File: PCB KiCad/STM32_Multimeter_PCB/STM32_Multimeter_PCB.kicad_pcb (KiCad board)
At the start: 2 copper layers, 128 parts, among them J1 Conn_01x02_Pin, J10 Conn_01x01_Pin, J11 Conn_01x01_Pin, J2 USB_B_Micro, J3 Conn_01x04_Pin, J4 Conn_Coaxial, J5 Conn_01x03_Pin, J7 Conn_01x02_Pin, J8 Conn_01x01_Pin, K1 G6K-2, Q1 AOD2810, Q10 BC327, Q11 BC327, Q12 BC327, Q13 BC327, Q14 BC327, Q15 BC327, Q2 AOD2810, Q3 AOD2810, Q4 AOD2810, Q5 AOD2810, Q6 BC327, Q7 BC327, Q8 BC327, Q9 BC327, SW1 SW_Push, SW3 SW_Push, SW4 SW_DPDT_x2, U1 STM32WB55CGUx, U10 AMS1117-3.3, U11 4051, U3 LTC4054XES5-4.2, U4 DW01A, U5 FS8205A, U9 TPS61040DBV, Y1 Crystal 32 MHz

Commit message: Routed Analog and Microcontroler section
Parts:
- D7, F1, J11, Q12, Q13, Q14, Q3, Q4, Q5, R16, R17, R18, R19, R25, R26, R38, R4, R41, R42, R43, R44, R45, R46, R47, R48: moved to B.Cu
- J1: footprint Connector_PinHeader_2.54mm:PinHeader_1x02_P2.54mm_Vertical -> moje_elementy:batt
- moved D7 195.8 mm to (76.7, 30.9), turned to 90 degrees
- moved R38 195.5 mm to (73.0, 32.4)
- moved R46 193.9 mm to (85.3, 34.4)
- moved R47 193.7 mm to (85.3, 31.5)
- moved R48 193.7 mm to (85.3, 28.5)
- moved R44 192.8 mm to (64.1, 41.7), turned to 180 degrees
- moved R26 192.5 mm to (64.1, 39.3), turned to 180 degrees
- moved R42 192.4 mm to (51.5, 41.7), turned to 180 degrees
- moved R41 192.4 mm to (38.8, 41.7), turned to 180 degrees
- moved R19 192.2 mm to (38.8, 39.4), turned to 180 degrees
- moved R25 192.1 mm to (51.5, 39.4), turned to 180 degrees
- moved Q12 192.0 mm to (38.9, 45.0), turned to -90 degrees
- moved Q13 189.1 mm to (51.7, 45.2), turned to -90 degrees
- moved Q14 189.0 mm to (64.2, 45.2), turned to -90 degrees
- moved R4 187.8 mm to (39.0, 48.2)
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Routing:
- net Net-(Q3-D): track 0.00 -> 54.4 mm
- net Net-(D4-A2): track 0.00 -> 34.2 mm
- net Net-(Q4-S): track 0.00 -> 29.5 mm
- net VDD: track 9.02 -> 29.8 mm
- net Net-(U1-PH3): track 0.00 -> 20.4 mm
- net +5V: track 0.00 -> 18.2 mm, vias 0 -> 2
- net Net-(J1-Pin_2): track 0.00 -> 18.1 mm
- net Net-(K1-Pad5): track 0.00 -> 16.7 mm
- net Net-(Q5-S): track 0.00 -> 16.3 mm
- net Net-(U1-PB7): track 0.00 -> 15.7 mm
- net Net-(K1-Pad7): track 0.00 -> 13.9 mm
- net Net-(U1-NRST): track 0.00 -> 13.7 mm
- net Net-(Q3-S): track 0.00 -> 12.8 mm
- net Net-(J1-Pin_1): track 0.00 -> 12.4 mm
- net GND: track 5.51 -> 15.8 mm
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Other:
- copper layers 2 -> 4

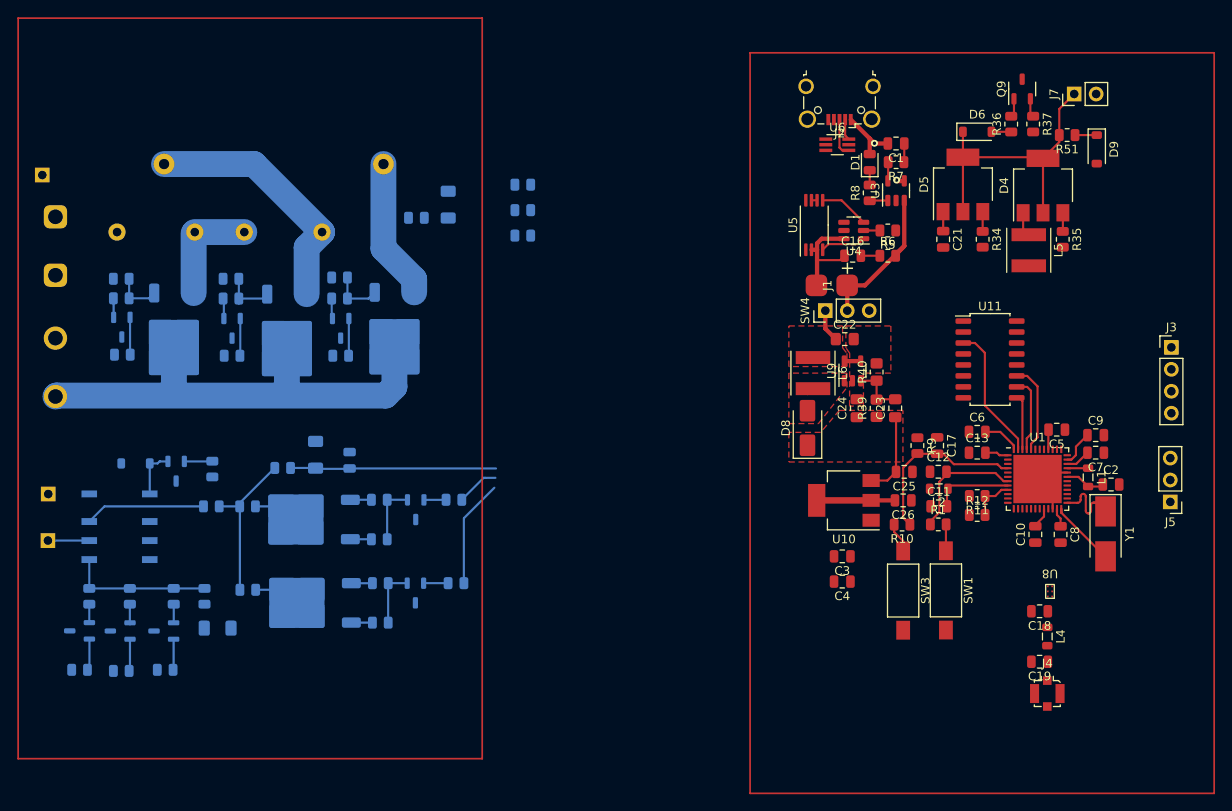
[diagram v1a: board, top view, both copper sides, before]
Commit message: routed out signals and power planes
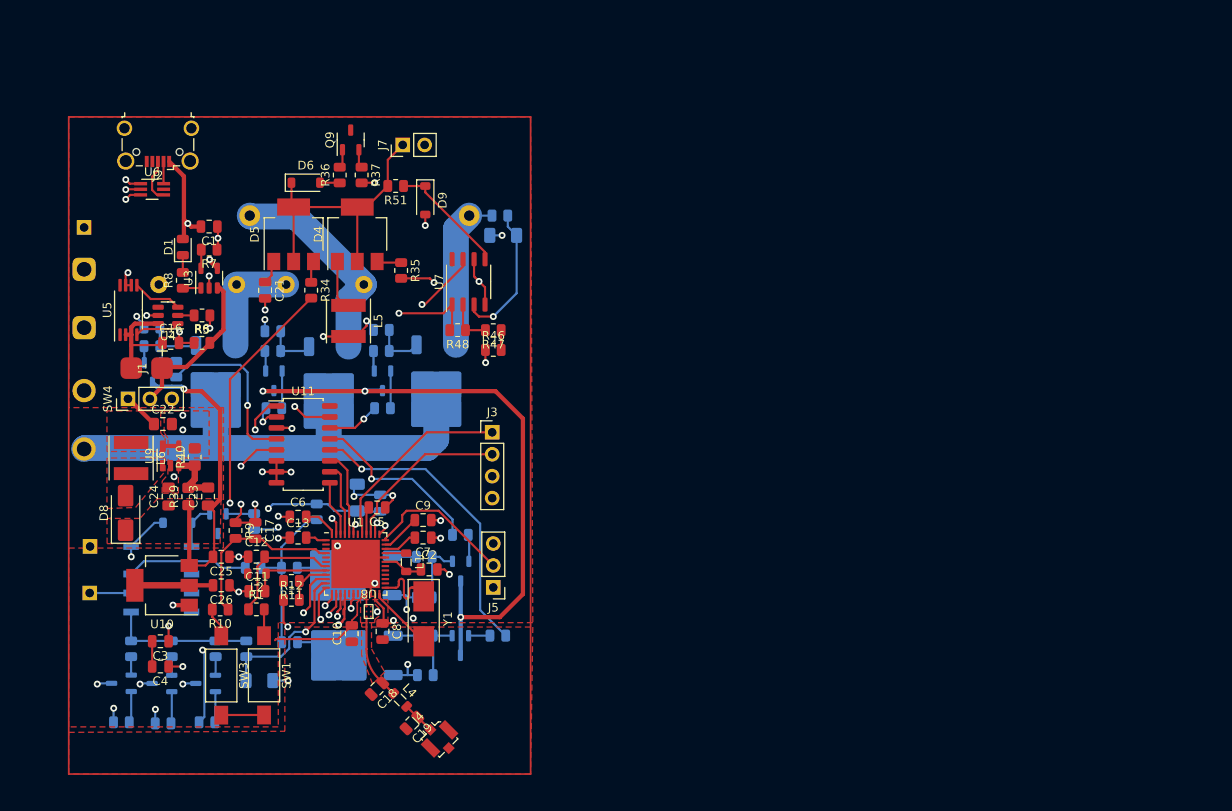
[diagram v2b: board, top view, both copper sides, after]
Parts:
- added U7: ~, Package_SO:SOP-8_3.9x4.9mm_P1.27mm, F.Cu at (79.1, 39.8)
- R46, R47, R48: moved to F.Cu
- moved SW4 81.4 mm to (39.6, 53.3)
- moved C24 80.3 mm to (44.3, 64.6)
- moved R39 80.3 mm to (46.6, 64.6)
- moved C23 80.2 mm to (48.9, 64.6)
- moved R7 80.2 mm to (49.0, 36.1)
- moved R8 80.2 mm to (46.0, 39.6)
- moved U3 80.2 mm to (49.0, 39.4)
- moved D1 80.1 mm to (46.0, 35.8)
- moved U11 80.1 mm to (59.9, 58.6)
- moved C1 80.1 mm to (49.0, 33.4)
- moved R6 80.0 mm to (48.2, 46.9)
- moved U5 80.0 mm to (39.7, 43.0)
- moved R5 80.0 mm to (48.2, 43.7)
- moved U4 80.0 mm to (44.3, 43.7)
- moved R11 80.0 mm to (58.5, 74.4)
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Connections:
- Q6 pad 3: VCC -> VDD
- Q7 pad 3: VCC -> VDD
- Q8 pad 3: VCC -> VDD
- Q9 pad 3: VCC -> VDD
- U11 pad 12: Range 100 to 10k ohm -> Range 1/100
- U11 pad 14: Range 1/100 -> Range 0,1A
- U11 pad 5: Range 0,1A -> Range 100 to 10k ohm
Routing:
- net +9V: track 9.79 -> 119.0 mm, vias 0 -> 4
- net GND: track 15.8 -> 96.6 mm, vias 0 -> 41
- net charge LC: track 0.00 -> 58.0 mm, vias 0 -> 2
- net Net-(U1-PA12): track 0.00 -> 56.4 mm, vias 0 -> 2
- net C on: track 0.00 -> 53.8 mm, vias 0 -> 2
- net Net-(U1-PA11): track 0.00 -> 53.5 mm, vias 0 -> 2
- net current input: track 0.00 -> 53.3 mm, vias 0 -> 2
- net Range 1 to 100 ohm: track 0.00 -> 52.4 mm, vias 0 -> 2
- net CL input: track 0.00 -> 50.6 mm, vias 0 -> 2
- net L on: track 0.00 -> 50.0 mm, vias 0 -> 2
- net Range 10k to 1kk ohm: track 0.00 -> 41.6 mm, vias 0 -> 2
- net Range 100 to 10k ohm: track 0.00 -> 39.8 mm, vias 0 -> 2
- net VDD: track 29.8 -> 60.4 mm, vias 0 -> 5
- net Net-(J3-Pin_1): track 0.00 -> 22.3 mm
- net Range 1/100: track 12.5 -> 34.5 mm, vias 0 -> 1
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- added copper zone on In1.Cu, net GND
- added copper zone on In2.Cu, net GND
- added copper zone on F.Cu, net VDD

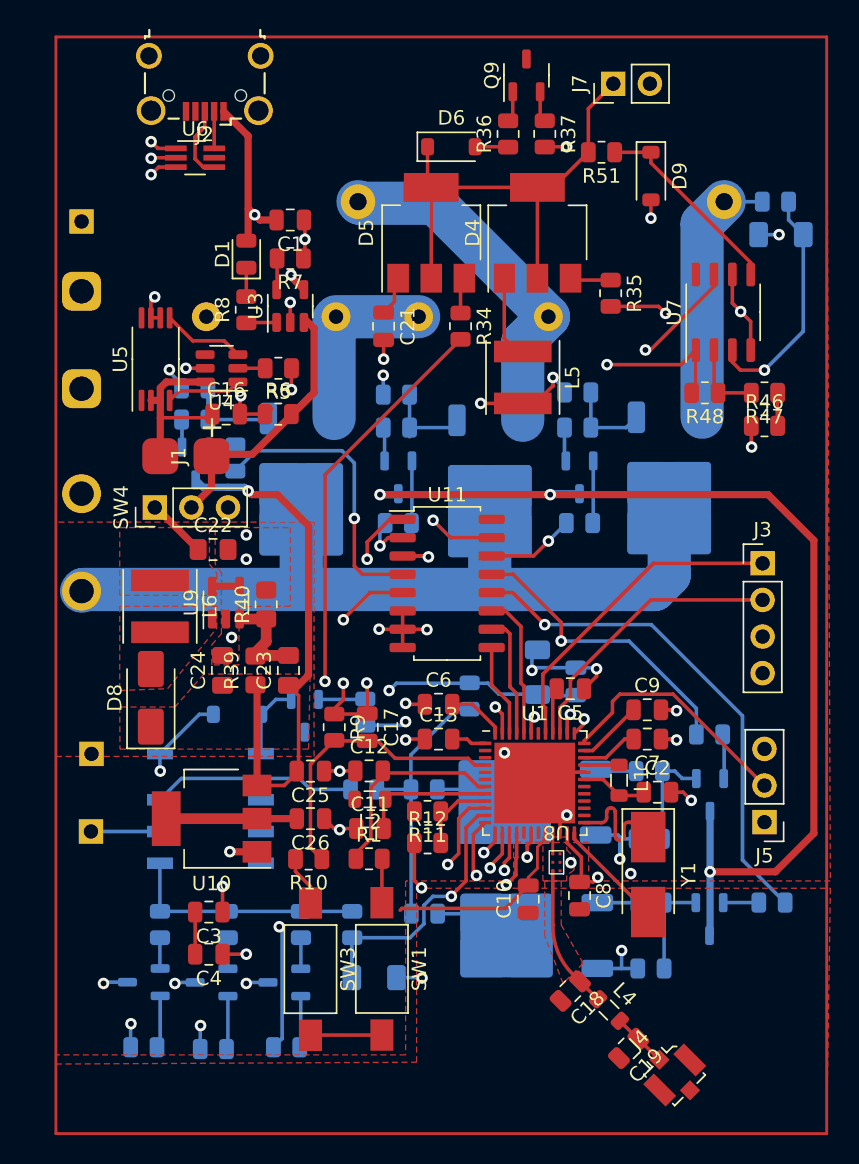
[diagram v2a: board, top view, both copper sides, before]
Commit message: added stiching via-s and impedance controled traces for RF
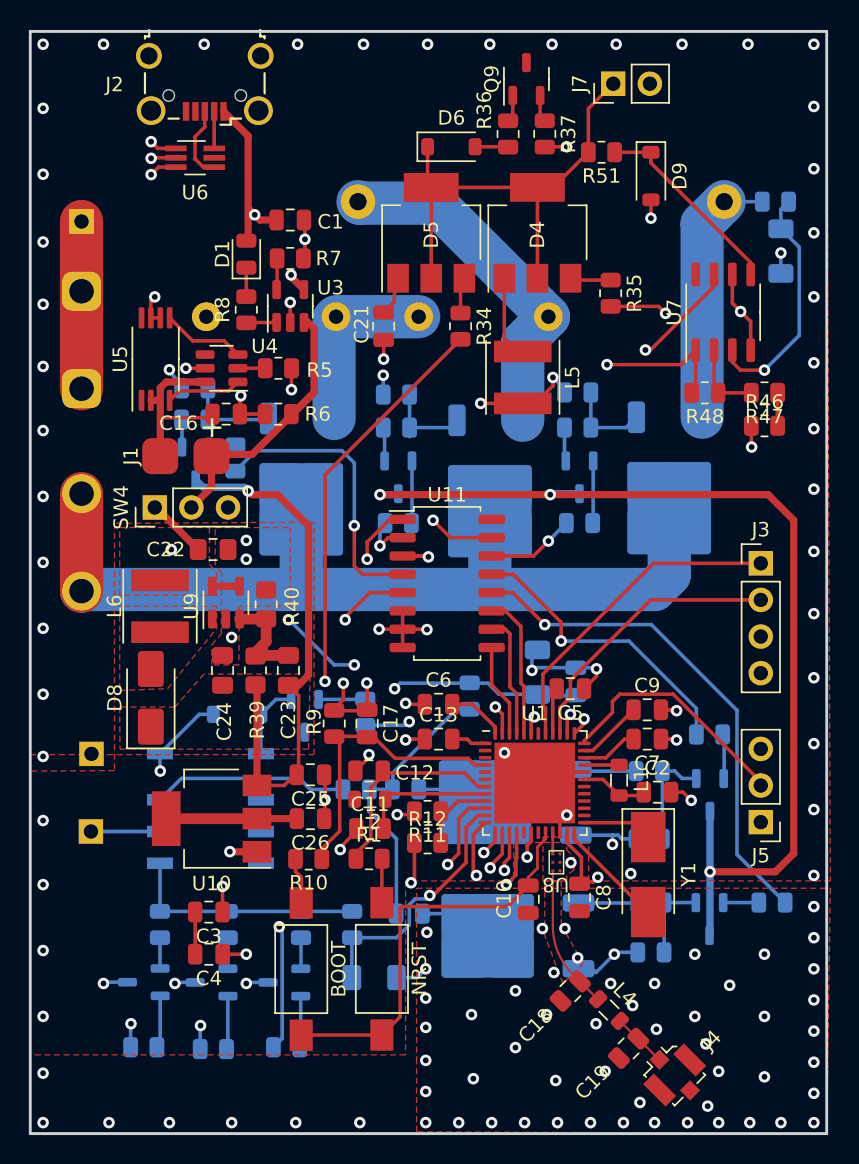
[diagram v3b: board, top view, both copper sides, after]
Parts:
- moved Q1 1.37 mm to (63.8, 73.8)
- moved Q2 1.31 mm to (64.0, 83.1)
- moved R20 1.28 mm to (57.0, 72.9)
- moved D7 1.14 mm to (83.1, 35.6), turned to -90 degrees
- moved R22 1.12 mm to (74.0, 84.2)
- moved R24 1.06 mm to (57.3, 81.5)
- moved BOOT 0.64 mm to (49.8, 85.4)
- moved R14 0.52 mm to (53.6, 72.9)
- moved C17 0.26 mm to (54.4, 68.3)
- moved R9 0.26 mm to (52.1, 68.3)
- moved C25 0.25 mm to (50.4, 71.9)
- moved J5 0.25 mm to (81.7, 75.2)
- moved Q9 0.25 mm to (65.4, 23.6)
- moved C8 0.13 mm to (69.1, 80.4)
- moved J3 0.13 mm to (81.7, 57.2)
- renumbered SW3 to BOOT, SW1 to NRST
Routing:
- net +BATT: track 6.12 -> 35.0 mm, vias 0 -> 4
- net Net-(J11-Pin_1): track 0.00 -> 11.6 mm
- net VDD: track 60.4 -> 70.9 mm
- net Net-(Q3-D): track 56.0 -> 62.7 mm
- net GND: track 96.6 -> 100.3 mm, vias 41 -> 140
- net Net-(U1-OSC_IN): track 8.40 -> 4.85 mm
- net Net-(Q2-D): track 4.15 -> 5.99 mm
- net Net-(Q1-G): track 2.80 -> 4.23 mm
- net Net-(Q2-G): track 2.81 -> 4.13 mm
- net Net-(Q1-D): track 4.23 -> 5.52 mm
- net +9V: track 119.0 -> 117.8 mm
- net Net-(Q10-C): track 6.65 -> 5.53 mm
- net R input: track 18.5 -> 17.8 mm
- net Range 1 to 100 ohm: track 52.4 -> 52.9 mm
- net Net-(K1-Pad7): track 14.1 -> 13.6 mm
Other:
- board outline added: 55.2 x 76.5 mm
